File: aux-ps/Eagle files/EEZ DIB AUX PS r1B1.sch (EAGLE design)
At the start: 111 parts, among them IC1 AMC6821SDBQR, IC2 VIPer35L, IC3 TL431, J1 PF0030/PC, J2 1-726388-2, J3 1-726388-2, J4 1-726388-2, J5 SWEB 8094 AU/GN, Q1 BTA26-600, Q2 BTA26-600, Q3 2N7002, Q4 2N7002, Q5 IRLL2705PBF, Q6 2N7002, SW1 DF62J12S2AHQA, X1 39-28-1063, X2 39-30-1039, X3 ZL231-16KG, X4 22-23-2031, X5 22-23-2021

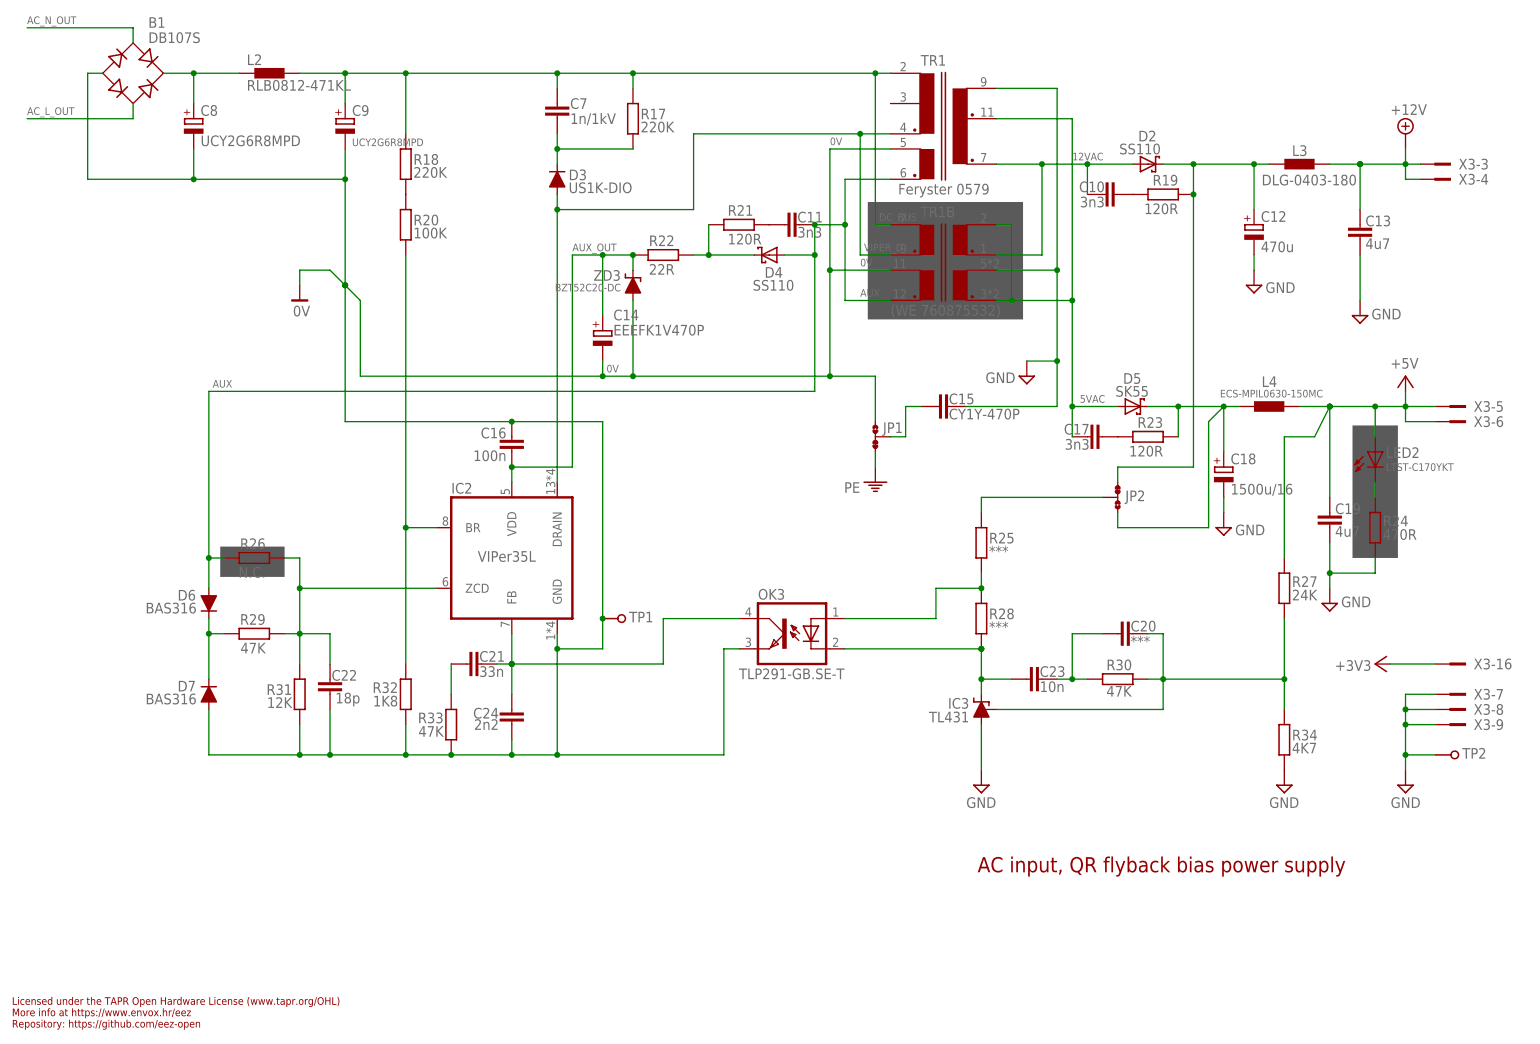
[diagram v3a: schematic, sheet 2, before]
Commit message: aux-ps SW1 adjustment
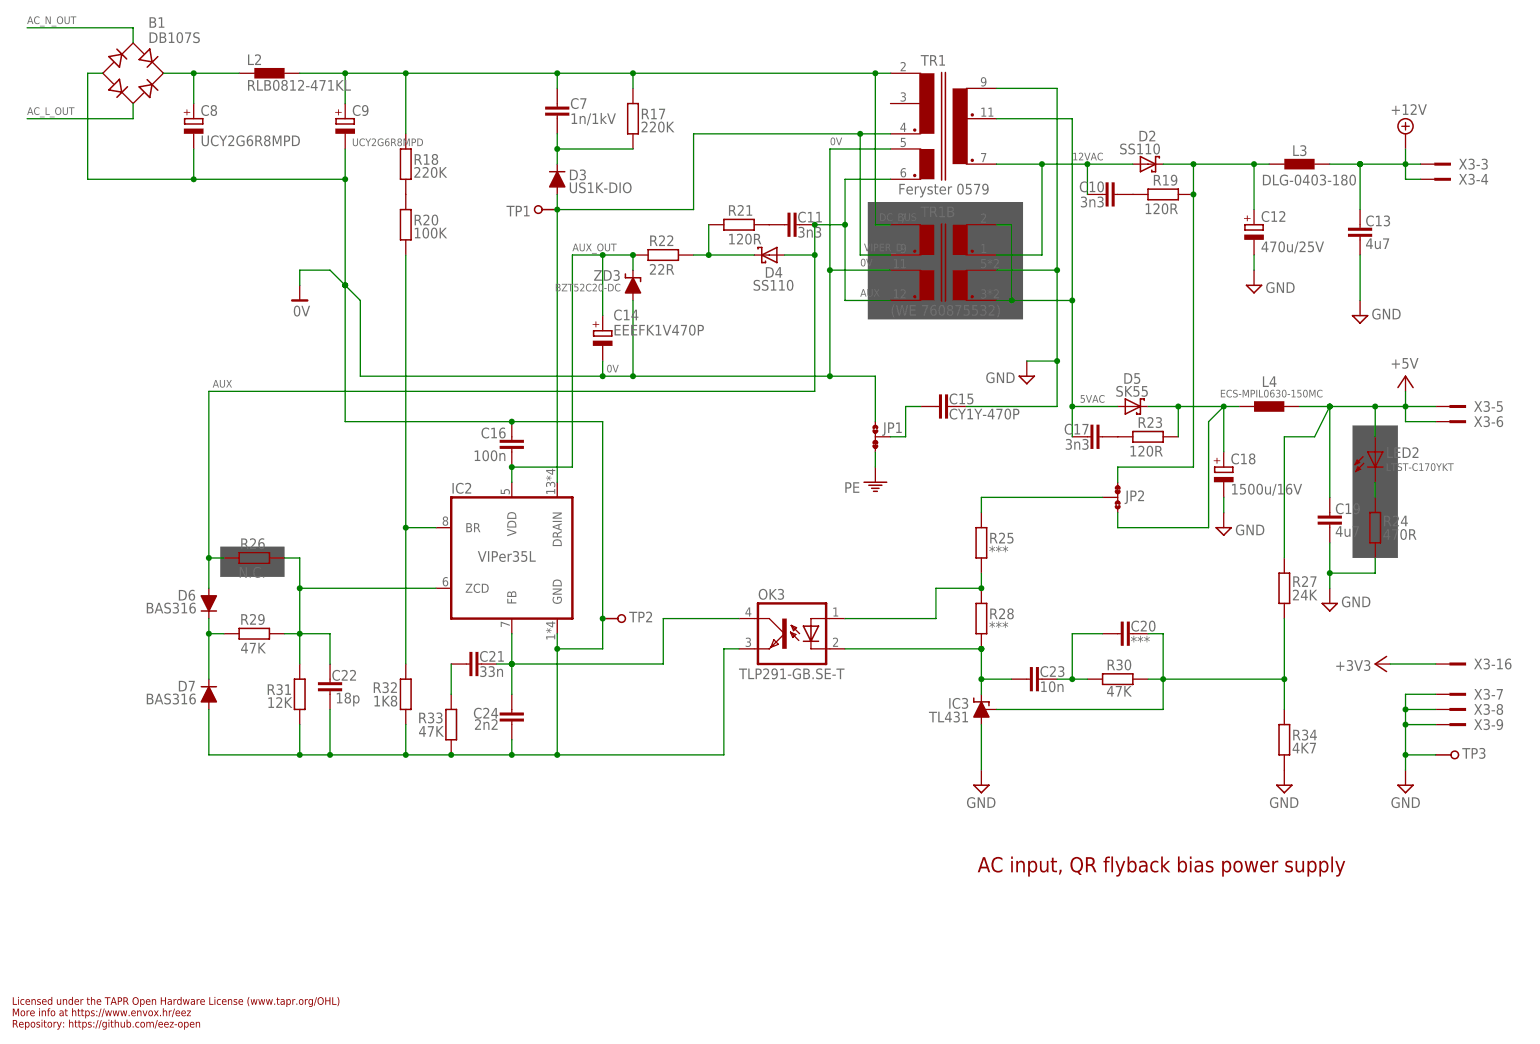
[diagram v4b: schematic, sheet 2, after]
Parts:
- added TP3: (no value), EEZ_Lib1:PCB_TEST_TABSHIELD
- C1, C2: value 47n/400V (X1) -> 47n/400V (X2)
- C12: value 470u -> 470u/25V
- C18: value 1500u/16 -> 1500u/16V
- Q5: value IRLL2705PBF -> BSP716NH6327XTSA1
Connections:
- net 0V: now also TP2.P$1; no longer TP1.P$1
- net GND: now also TP3.P$1; no longer TP2.P$1
- net VIPER_D: now also TP1.P$1
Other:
- moved on the sheet: TP1, TP2
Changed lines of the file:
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@@
 <part name="VAR2" library="EEZ_Lib1" deviceset="VARISTOR" device="-13" value="ERZE14A431"/>
 <part name="VAR1" library="EEZ_Lib1" deviceset="VARISTOR" device="-13" value="ERZE14A431"/>
-<part name="C1" library="rcl" deviceset="C-EU" device="102-054X133" value="47n/400V (X1)"/>
+<part name="C1" library="rcl" deviceset="C-EU" device="102-054X133" value="47n/400V (X2)"/>
 <part name="TR1B" library="EEZ_Lib1" deviceset="WE-UOST" device="" value="(WE 760875532)"/>
 <part name="R8" library="rcl" deviceset="R-EU_" device="R2512" value="330R/2W"/>
@@
 <part name="R3" library="rcl" deviceset="R-EU_" device="R0805" value="220R"/>
 <part name="R10" library="rcl" deviceset="R-EU_" device="R2512" value="330R/2W"/>
-<part name="C2" library="rcl" deviceset="C-EU" device="102-054X133" value="47n/400V (X1)"/>
+<part name="C2" library="rcl" deviceset="C-EU" device="102-054X133" value="47n/400V (X2)"/>
 <part name="OK1" library="EEZ_Lib1" deviceset="MOC305X" device="" value="MOC3052"/>
 <part name="OK2" library="optocoupler" deviceset="MOC30*" device="S" technology="33" value="MOC3062">
@@
 <part name="X4" library="con-molex" deviceset="22-23-2031" device=""/>
 <part name="D1" library="EEZ_Lib1" deviceset="SCHOTTKY" device="SOD123" value="SKL16"/>
-<part name="Q5" library="transistor-power" deviceset="N-HEXFET-2D_?-*" device="SOT232" technology="IRLL014N" value="IRLL2705PBF"/>
+<part name="Q5" library="transistor-power" deviceset="N-HEXFET-2D_?-*" device="SOT232" technology="IRLL014N" value="BSP716NH6327XTSA1"/>
 <part name="R11" library="rcl" deviceset="R-EU_" device="R0805" value="2K2"/>
 <part name="R15" library="rcl" deviceset="R-EU_" device="R0805" value="10K"/>
@@
 <part name="+3V1" library="supply1" deviceset="+3V3" device=""/>
 <part name="X5" library="con-molex" deviceset="22-23-2021" device=""/>
-<part name="TP1" library="EEZ_Lib1" deviceset="PCB_TEST_TAB" device="SHIELD"/>
+<part name="TP2" library="EEZ_Lib1" deviceset="PCB_TEST_TAB" device="SHIELD"/>
 <part name="L4" library="EEZ_inductors_and_transformers" deviceset="DE0704" device="" value="ECS-MPIL0630-150MC"/>
 <part name="D5" library="EEZ_Lib1" deviceset="SCHOTTKY" device="SMB" value="SK55"/>
@@
 <part name="C14" library="EEZ_Lib1" deviceset="ECAP" device="PANASONIC_H" value="EEEFK1V470P"/>
 <part name="SUPPLY15" library="supply2" deviceset="GND" device=""/>
-<part name="C18" library="EEZ_Lib1" deviceset="ECAP" device="5G_13MM" value="1500u/16"/>
+<part name="C18" library="EEZ_Lib1" deviceset="ECAP" device="5G_13MM" value="1500u/16V"/>
 <part name="SUPPLY2" library="supply2" deviceset="GND" device=""/>
 <part name="P+2" library="supply1" deviceset="+5V" device=""/>
@@
 <part name="SUPPLY4" library="supply2" deviceset="GND" device=""/>
 <part name="SUPPLY5" library="supply2" deviceset="GND" device=""/>
-<part name="C12" library="EEZ_Lib1" deviceset="ECAP" device="5G_10.5MM" value="470u"/>
+<part name="C12" library="EEZ_Lib1" deviceset="ECAP" device="5G_10.5MM" value="470u/25V"/>
 <part name="IC3" library="EEZ_Lib1" deviceset="TL431" device="" value="TL431"/>
 <part name="C23" library="rcl" deviceset="C-EU" device="C0805" value="10n"/>
@@
 <part name="J3" library="EEZ_connectors" deviceset="PCB_TAB" device="4.8MM" value="1-726388-2"/>
 <part name="J4" library="EEZ_connectors" deviceset="PCB_TAB" device="4.8MM" value="1-726388-2"/>
-<part name="TP2" library="EEZ_Lib1" deviceset="PCB_TEST_TAB" device="SHIELD"/>
+<part name="TP3" library="EEZ_Lib1" deviceset="PCB_TEST_TAB" device="SHIELD"/>
+<part name="TP1" library="EEZ_Lib1" deviceset="PCB_TEST_TAB" device="SHIELD"/>
 </parts>
 <sheets>
@@
 <attribute name="VALUE" x="104.648" y="127.254" size="1.27" layer="96" rot="R180"/>
 </instance>
-<instance part="TP1" gate="G$1" x="104.14" y="71.12" smashed="yes">
+<instance part="TP2" gate="G$1" x="104.14" y="71.12" smashed="yes">
 <attribute name="NAME" x="106.045" y="70.485" size="1.778" layer="95"/>
 <attribute name="VALUE" x="104.14" y="68.58" size="1.778" layer="96"/>
@@
 <attribute name="NAME" x="189.23" y="90.805" size="1.778" layer="95"/>
 </instance>
-<instance part="TP2" gate="G$1" x="243.84" y="48.26" smashed="yes">
+<instance part="TP3" gate="G$1" x="243.84" y="48.26" smashed="yes">
 <attribute name="NAME" x="245.745" y="47.625" size="1.778" layer="95"/>
 <attribute name="VALUE" x="243.84" y="45.72" size="1.778" layer="96"/>
+</instance>
+<instance part="TP1" gate="G$1" x="91.44" y="139.7" smashed="yes" rot="R180">
+<attribute name="NAME" x="89.535" y="140.335" size="1.778" layer="95" rot="R180"/>
+<attribute name="VALUE" x="91.44" y="142.24" size="1.778" layer="96" rot="R180"/>
 </instance>
 </instances>
@@
 <junction x="93.98" y="139.7"/>
 <label x="145.415" y="132.715" size="1.27" layer="102"/>
+<pinref part="TP1" gate="G$1" pin="P$1"/>
 </segment>
 </net>
@@
 <wire x1="241.3" y1="53.34" x2="236.22" y2="53.34" width="0.1524" layer="91"/>
 <junction x="236.22" y="53.34"/>
-<pinref part="TP2" gate="G$1" pin="P$1"/>
+<pinref part="TP3" gate="G$1" pin="P$1"/>
 <wire x1="241.3" y1="48.26" x2="236.22" y2="48.26" width="0.1524" layer="91"/>
 <junction x="236.22" y="48.26"/>
@@
 <wire x1="93.98" y1="66.04" x2="93.98" y2="48.26" width="0.1524" layer="91"/>
 <junction x="93.98" y="48.26"/>
-<pinref part="TP1" gate="G$1" pin="P$1"/>
+<pinref part="TP2" gate="G$1" pin="P$1"/>
 <junction x="101.6" y="71.12"/>
 <wire x1="101.6" y1="111.76" x2="60.96" y2="111.76" width="0.1524" layer="91"/>
